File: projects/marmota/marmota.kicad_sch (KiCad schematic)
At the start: 51 parts, among them J1 USB_C, J2 Conn_01x20_Pin, J3 Conn_01x20_Pin, SW1 Button top, SW2 Button side, U1 RP2040, U2 FLASH, U3 MCP73871, U4 RT6160, U5 ESP32, Y1 12MHz

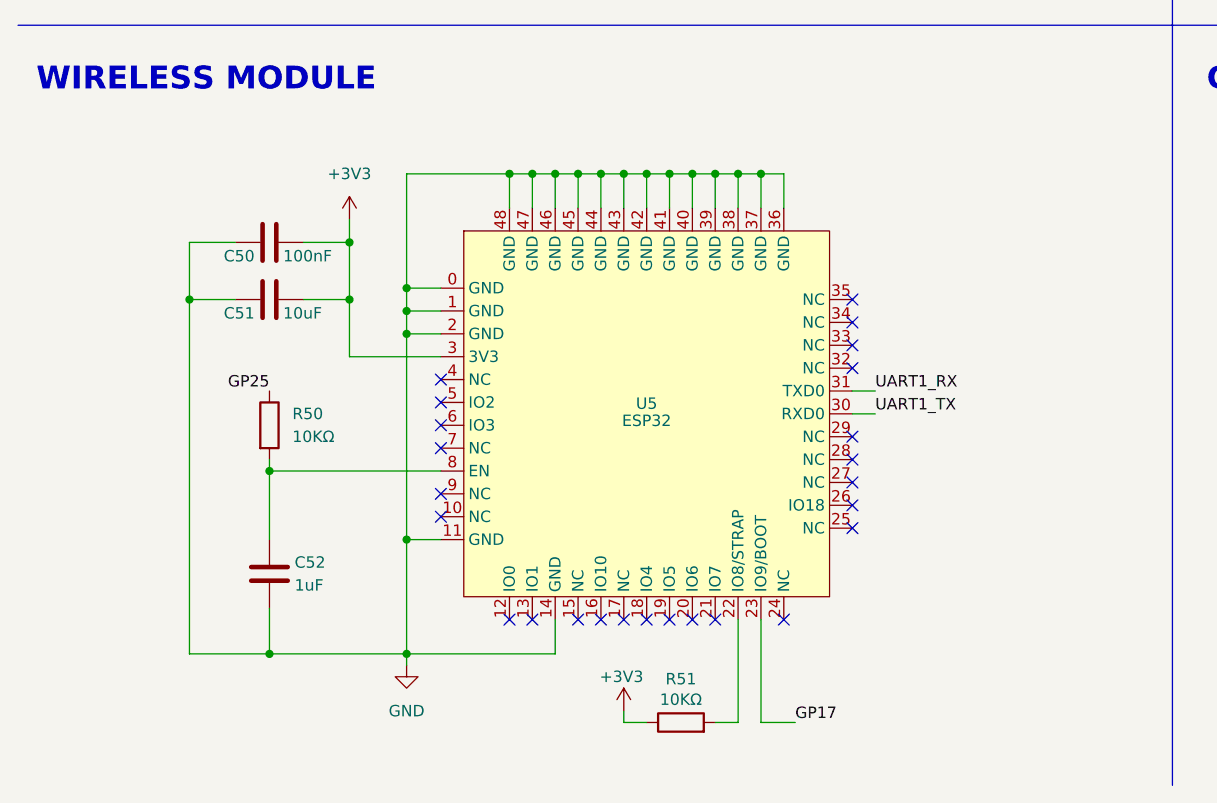
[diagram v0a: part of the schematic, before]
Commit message: Voltage divider and read on the ESP, Thermal relief for the ESP
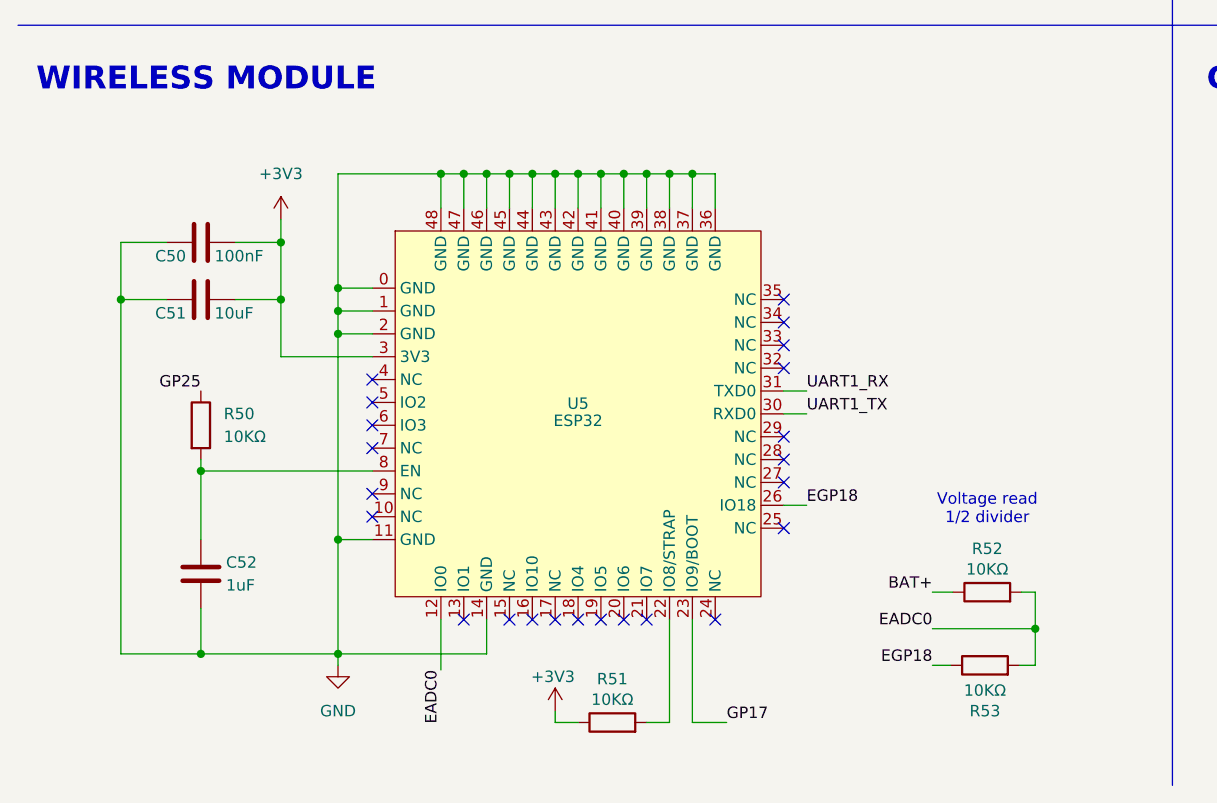
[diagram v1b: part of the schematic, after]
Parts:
- added R52, R53: 10KΩ, ILO_fp:0402_compact, symbol Device:R
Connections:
- net BAT+: now also R52.1
- net EADC0: now reaches U5.12 (IO0)
- net EADC0: now also R52.2, R53.2
- net EGP18: now reaches U5.26 (IO18)
- net EGP18: now also R53.1
- no-connect marks 37 -> 35
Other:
- note added: "Voltage read 1/2 divider"
- moved on the sheet: C50, C51, C52, R50, R51, U5

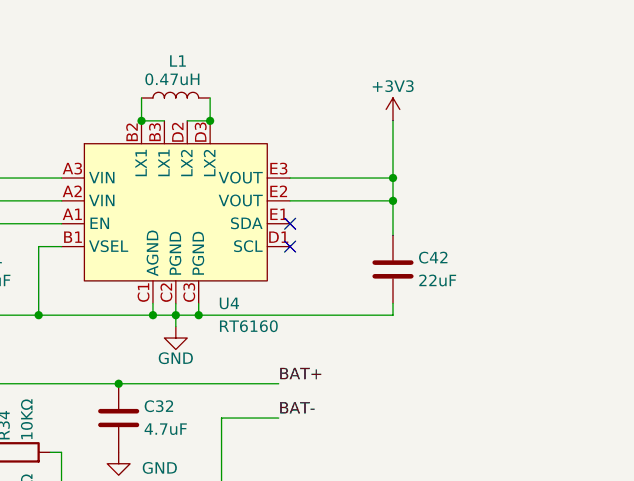
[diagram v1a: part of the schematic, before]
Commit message: New arrangement for buckboost, Added 2nd vcc capacitor
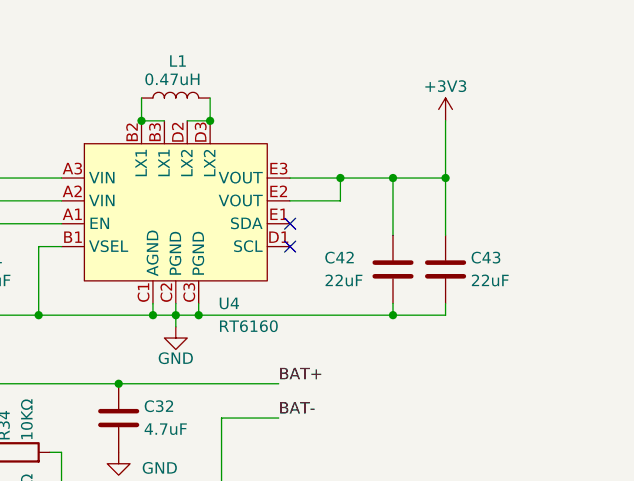
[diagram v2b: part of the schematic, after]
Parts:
- added C43: 22uF, ILO_fp:0402_compact, symbol Device:C
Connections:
- net +3V3: now also C43.2
- net GND: now also C43.1
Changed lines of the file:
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@@
 	)
 	(junction
+		(at 318.77 45.72)
+		(diameter 0)
+		(color 0 0 0 0)
+	)
+	(junction
 		(at 179.07 43.18)
 		(diameter 0)
@@
 	)
 	(junction
+		(at 312.928 30.48)
+		(diameter 0)
+		(color 0 0 0 0)
+	)
+	(junction
 		(at 279.4 45.72)
 		(diameter 0)
@@
 	)
 	(junction
-		(at 69.85 27.94)
+		(at 318.77 30.48)
 		(diameter 0)
 		(color 0 0 0 0)
 	)
 	(junction
-		(at 66.04 46.99)
+		(at 69.85 27.94)
 		(diameter 0)
 		(color 0 0 0 0)
 	)
 	(junction
-		(at 318.77 30.48)
+		(at 66.04 46.99)
 		(diameter 0)
 		(color 0 0 0 0)
@@
 	)
 	(junction
-		(at 318.77 33.02)
+		(at 324.612 30.48)
 		(diameter 0)
 		(color 0 0 0 0)
@@
 	(wire
 		(pts
+			(xy 324.612 30.48) (xy 324.612 36.83)
+		)
+		(stroke
+			(width 0)
+			(type default)
+		)
+	)
+	(wire
+		(pts
 			(xy 269.24 30.48) (xy 281.94 30.48)
 		)
@@
 	(wire
 		(pts
+			(xy 312.928 30.48) (xy 312.928 33.02)
+		)
+		(stroke
+			(width 0)
+			(type default)
+		)
+	)
+	(wire
+		(pts
 			(xy 182.88 26.67) (xy 182.88 27.94)
 		)
@@
 	(wire
 		(pts
-			(xy 318.77 30.48) (xy 318.77 33.02)
-		)
-		(stroke
-			(width 0)
-			(type default)
-		)
-	)
-	(wire
-		(pts
 			(xy 93.98 74.93) (xy 92.71 74.93)
 		)
@@
 	(wire
 		(pts
+			(xy 312.928 30.48) (xy 318.77 30.48)
+		)
+		(stroke
+			(width 0)
+			(type default)
+		)
+	)
+	(wire
+		(pts
 			(xy 68.58 46.99) (xy 71.12 46.99)
 		)
@@
 	(wire
 		(pts
+			(xy 318.77 30.48) (xy 318.77 36.83)
+		)
+		(stroke
+			(width 0)
+			(type default)
+		)
+	)
+	(wire
+		(pts
 			(xy 294.64 44.45) (xy 294.64 45.72)
 		)
@@
 	(wire
 		(pts
+			(xy 324.612 24.13) (xy 324.612 30.48)
+		)
+		(stroke
+			(width 0)
+			(type default)
+		)
+	)
+	(wire
+		(pts
 			(xy 64.77 166.37) (xy 64.77 170.18)
 		)
@@
 	(wire
 		(pts
+			(xy 307.34 33.02) (xy 312.928 33.02)
+		)
+		(stroke
+			(width 0)
+			(type default)
+		)
+	)
+	(wire
+		(pts
 			(xy 35.56 81.28) (xy 36.83 81.28)
 		)
@@
 	(wire
 		(pts
-			(xy 318.77 33.02) (xy 318.77 36.83)
-		)
-		(stroke
-			(width 0)
-			(type default)
-		)
-	)
-	(wire
-		(pts
 			(xy 237.49 63.5) (xy 234.95 63.5)
 		)
@@
 	(wire
 		(pts
-			(xy 307.34 30.48) (xy 318.77 30.48)
+			(xy 307.34 30.48) (xy 312.928 30.48)
 		)
 		(stroke
@@
 	(wire
 		(pts
-			(xy 307.34 33.02) (xy 318.77 33.02)
+			(xy 33.02 198.12) (xy 33.02 199.39)
 		)
 		(stroke
@@
 	(wire
 		(pts
-			(xy 33.02 198.12) (xy 33.02 199.39)
+			(xy 45.72 43.18) (xy 50.8 43.18)
 		)
 		(stroke
@@
 	(wire
 		(pts
-			(xy 45.72 43.18) (xy 50.8 43.18)
+			(xy 92.71 102.87) (xy 93.98 102.87)
 		)
 		(stroke
@@
 	(wire
 		(pts
-			(xy 92.71 102.87) (xy 93.98 102.87)
+			(xy 41.91 171.45) (xy 41.91 173.99)
 		)
 		(stroke
@@
 	(wire
 		(pts
-			(xy 41.91 171.45) (xy 41.91 173.99)
+			(xy 59.69 166.37) (xy 59.69 170.18)
 		)
 		(stroke
@@
 	(wire
 		(pts
-			(xy 59.69 166.37) (xy 59.69 170.18)
+			(xy 318.77 45.72) (xy 324.612 45.72)
 		)
 		(stroke
@@
 	(wire
 		(pts
+			(xy 324.612 45.72) (xy 324.612 44.45)
+		)
+		(stroke
+			(width 0)
+			(type default)
+		)
+	)
+	(wire
+		(pts
 			(xy 128.27 138.43) (xy 128.27 140.97)
 		)
@@
 	(wire
 		(pts
-			(xy 318.77 24.13) (xy 318.77 30.48)
-		)
-		(stroke
-			(width 0)
-			(type default)
-		)
-	)
-	(wire
-		(pts
 			(xy 124.206 212.852) (xy 125.73 212.852)
 		)
@@
 	(wire
 		(pts
+			(xy 318.77 30.48) (xy 324.612 30.48)
+		)
+		(stroke
+			(width 0)
+			(type default)
+		)
+	)
+	(wire
+		(pts
 			(xy 111.76 138.43) (xy 111.76 140.97)
 		)
@@
 	(symbol
 		(lib_id "power:+3V3")
-		(at 318.77 24.13 0)
+		(at 324.612 24.13 0)
 		(unit 1)
 		(exclude_from_sim no)
@@
 		(dnp no)
 		(property "Reference" "#PWR048"
-			(at 318.77 27.94 0)
+			(at 324.612 27.94 0)
 			(effects
 				(font
@@
 		)
 		(property "Value" "+3V3"
-			(at 318.77 20.32 0)
+			(at 324.612 20.32 0)
 			(effects
 				(font
@@
 		)
 		(property "Footprint" ""
-			(at 318.77 24.13 0)
+			(at 324.612 24.13 0)
 			(effects
 				(font
@@
 		)
 		(property "Datasheet" ""
-			(at 318.77 24.13 0)
+			(at 324.612 24.13 0)
 			(effects
 				(font
@@
 		)
 		(property "Description" "Power symbol creates a global label with name \"+3V3\""
-			(at 318.77 24.13 0)
+			(at 324.612 24.13 0)
 			(effects
 				(font
@@
 		(dnp no)
 		(property "Reference" "C42"
-			(at 321.564 39.37 0)
+			(at 311.15 39.37 0)
 			(effects
 				(font
@@
 		)
 		(property "Value" "22uF"
-			(at 321.564 41.91 0)
+			(at 311.15 41.91 0)
 			(effects
 				(font
@@
 					(unit 1)
 				)
+			)
+		)
+	)
+	(symbol
+		(lib_id "Device:C")
+		(at 324.612 40.64 180)
+		(unit 1)
+		(exclude_from_sim no)
+		(in_bom yes)
+		(on_board yes)
+		(dnp no)
+		(property "Reference" "C43"
+			(at 327.406 39.37 0)
+			(effects
+				(font
+					(size 1.27 1.27)
+				)
+				(justify right)
+			)
+		)
+		(property "Value" "22uF"
+			(at 327.406 41.91 0)
+			(effects
+				(font
+					(size 1.27 1.27)
+				)
+				(justify right)
+			)
+		)
+		(property "Footprint" "ILO_fp:0402_compact"
+			(at 323.6468 36.83 0)
+			(effects
+				(font
+					(size 1.27 1.27)
+				)
+				(hide yes)
+			)
+		)
+		(property "Datasheet" "~"
+			(at 324.612 40.64 0)
+			(effects
+				(font
+					(size 1.27 1.27)
+				)
+				(hide yes)
+			)
+		)
+		(property "Description" "Unpolarized capacitor"
+			(at 324.612 40.64 0)
+			(effects
+				(font
+					(size 1.27 1.27)
+				)
+				(hide yes)
+			)
+		)
+		(property "LCSC" "C105226"
+			(at 324.612 40.64 0)
+			(effects
+				(font
+					(size 1.27 1.27)
+				)
+				(hide yes)
+			)
+		)
+		(property "Export" "yes"
+			(at 324.612 40.64 0)
+			(effects
+				(font
+					(size 1.27 1.27)
+				)
+				(hide yes)
+			)
+		)
+		(property "Group" "C"
+			(at 324.612 40.64 0)
+			(effects
+				(font
+					(size 1.27 1.27)
+				)
+				(hide yes)
+			)
+		)
+		(property "Mount" "SMD"
+			(at 324.612 40.64 0)
+			(effects
+				(font
+					(size 1.27 1.27)
+				)
+				(hide yes)
+			)
+		)
+		(pin "2"
+		)
+		(pin "1"
+		)
+		(instances
+			(project "marmota"
+				(path "/752a740b-2d20-4431-a887-abcf944e2ab4"
+					(reference "C43")
+					(unit 1)
+				)

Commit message: Added I2C pullups
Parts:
- added R7, R8: 4.7KΩ, ILO_fp:0402_compact, symbol Device:R
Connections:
- net +3V3: now also R7.2, R8.2
- net I2C_SCL: now also R8.1
- net I2C_SDA: now also R7.1
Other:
- note added: "Analog filtering"
- note added: "Board LED"
- note added: "Controlled from RP2040"
- note added: "Flash and comms from/to RP2040"
- note added: "I2C pull-up"
- note added: "Reset"
- moved on the sheet: C50, C51, C61, C62, C63, C64, D1, R6

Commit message: Bigger footprint inductor
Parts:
- L1: footprint ILO_fp:0603_compact -> ILO_fp:SMD_16x10; LCSC C341701 -> C5832340
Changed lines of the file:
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@@
 			)
 		)
-		(property "Footprint" "ILO_fp:0603_compact"
+		(property "Footprint" "ILO_fp:SMD_16x10"
 			(at 294.64 21.59 0)
 			(effects
@@
 			)
 		)
-		(property "LCSC" "C341701"
+		(property "LCSC" "C5832340"
 			(at 294.64 21.59 0)
 			(effects

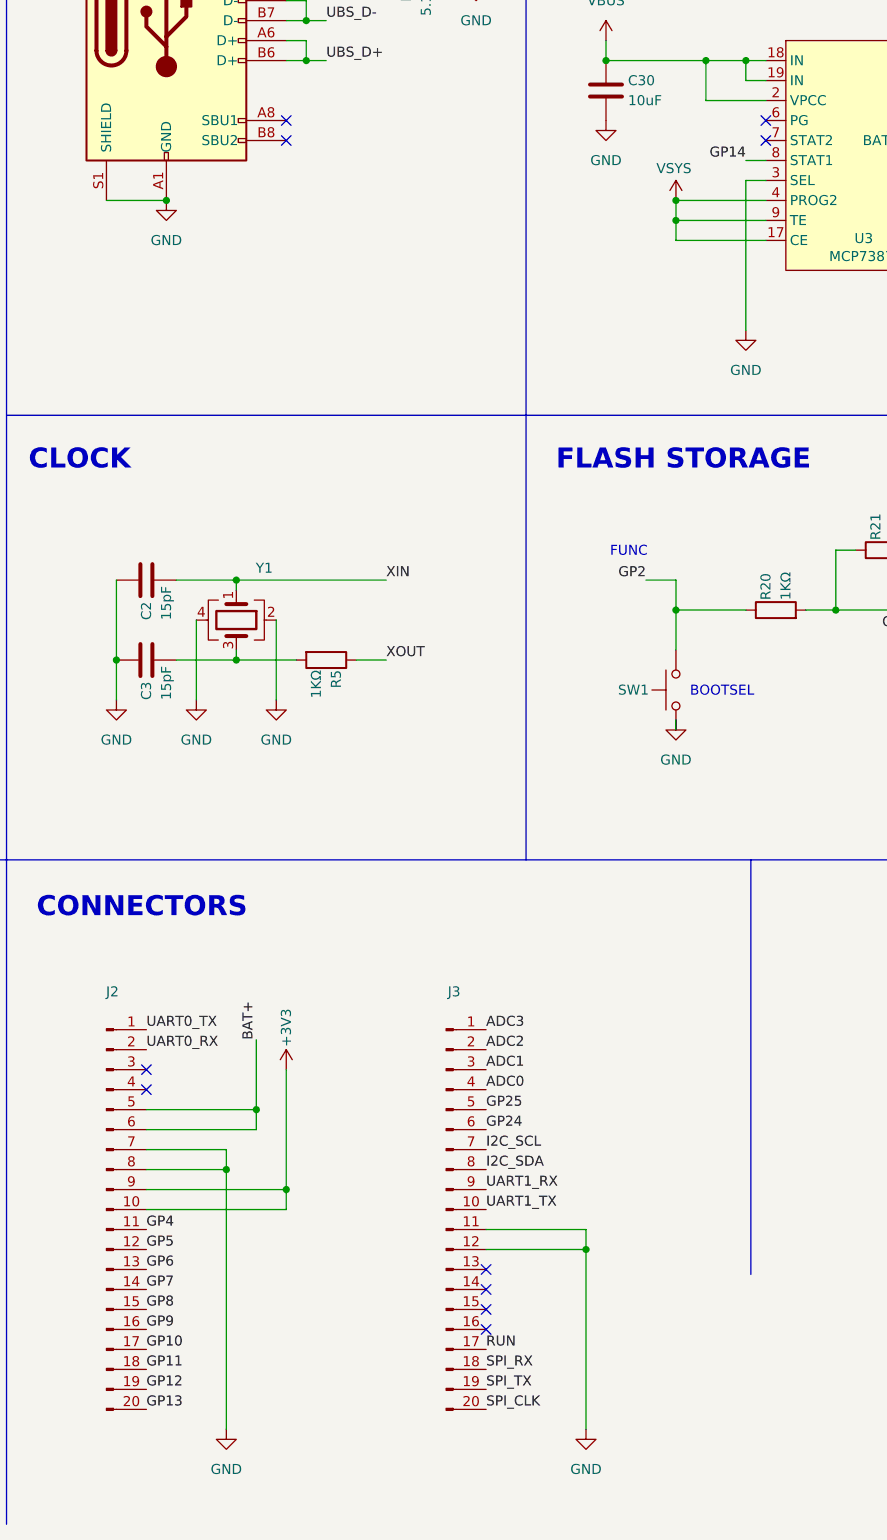
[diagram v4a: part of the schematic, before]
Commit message: Extra GPIO exposed to connector, Ground plane tweaks
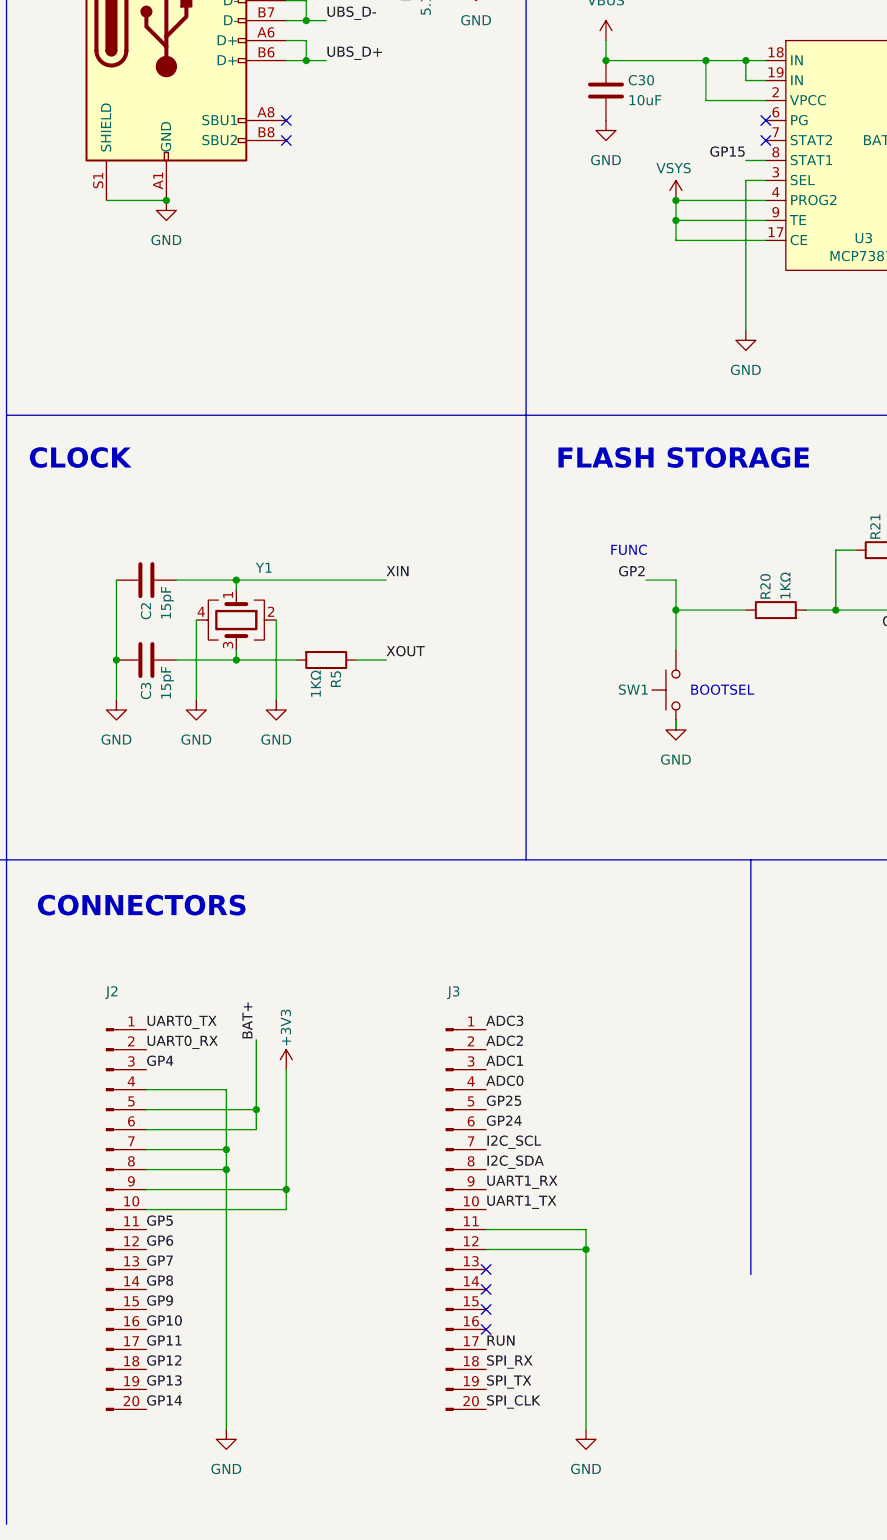
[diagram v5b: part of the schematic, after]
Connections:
- net GND: now also J2.4 (Pin_4)
- net GP10: now also J2.16 (Pin_16); no longer J2.17 (Pin_17)
- net GP11: now also J2.17 (Pin_17); no longer J2.18 (Pin_18)
- net GP12: now also J2.18 (Pin_18); no longer J2.19 (Pin_19)
- net GP13: now also J2.19 (Pin_19); no longer J2.20 (Pin_20)
- net GP14: now also J2.20 (Pin_20); no longer U3.8 (STAT1)
- net GP15: now also U3.8 (STAT1)
- net GP4: now also J2.3 (Pin_3); no longer J2.11 (Pin_11)
- net GP5: now also J2.11 (Pin_11); no longer J2.12 (Pin_12)
- net GP6: now also J2.12 (Pin_12); no longer J2.13 (Pin_13)
- net GP7: now also J2.13 (Pin_13); no longer J2.14 (Pin_14)
- net GP8: now also J2.14 (Pin_14); no longer J2.15 (Pin_15)
- net GP9: now also J2.15 (Pin_15); no longer J2.16 (Pin_16)
- no-connect marks 35 -> 33
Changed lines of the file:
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@@
 	)
 	(junction
+		(at 168.91 186.69)
+		(diameter 0)
+		(color 0 0 0 0)
+	)
+	(junction
 		(at 63.5 46.99)
 		(diameter 0)
@@
 	)
 	(no_connect
-		(at 158.75 179.07)
-	)
-	(no_connect
 		(at 237.49 55.88)
 	)
@@
 	)
 	(no_connect
-		(at 158.75 176.53)
-	)
-	(no_connect
 		(at 52.07 196.85)
 	)
@@
 	(wire
 		(pts
+			(xy 168.91 179.07) (xy 168.91 186.69)
+		)
+		(stroke
+			(width 0)
+			(type default)
+		)
+	)
+	(wire
+		(pts
 			(xy 87.63 166.37) (xy 87.63 170.18)
 		)
@@
 	(wire
 		(pts
+			(xy 158.75 179.07) (xy 168.91 179.07)
+		)
+		(stroke
+			(width 0)
+			(type default)
+		)
+	)
+	(wire
+		(pts
 			(xy 92.71 135.89) (xy 113.03 135.89)
 		)
@@
 		)
 	)
-	(label "GP11"
+	(label "GP12"
 		(at 158.75 214.63 0)
 		(fields_autoplaced yes)
@@
 		)
 	)
-	(label "GP13"
+	(label "GP14"
 		(at 158.75 219.71 0)
 		(fields_autoplaced yes)
@@
 		)
 	)
-	(label "GP6"
+	(label "GP7"
 		(at 158.75 201.93 0)
 		(fields_autoplaced yes)
@@
 		)
 	)
+	(label "GP4"
+		(at 158.75 176.53 0)
+		(fields_autoplaced yes)
+		(effects
+			(font
+				(size 1.27 1.27)
+			)
+			(justify left bottom)
+		)
+	)
 	(label "GP11"
 		(at 93.98 92.71 0)
@@
 		)
 	)
-	(label "GP5"
+	(label "GP6"
 		(at 158.75 199.39 0)
 		(fields_autoplaced yes)
@@
 		)
 	)
-	(label "GP7"
+	(label "GP8"
 		(at 158.75 204.47 0)
 		(fields_autoplaced yes)
@@
 		)
 	)
-	(label "GP8"
+	(label "GP9"
 		(at 158.75 207.01 0)
 		(fields_autoplaced yes)
@@
 		)
 	)
-	(label "GP4"
+	(label "GP5"
 		(at 158.75 196.85 0)
 		(fields_autoplaced yes)
@@
 		)
 	)
-	(label "GP9"
+	(label "GP10"
 		(at 158.75 209.55 0)
 		(fields_autoplaced yes)
@@
 		)
 	)
-	(label "GP14"
+	(label "GP15"
 		(at 234.95 60.96 180)
 		(fields_autoplaced yes)
@@
 		)
 	)
-	(label "GP12"
+	(label "GP13"
 		(at 158.75 217.17 0)
 		(fields_autoplaced yes)
@@
 		)
 	)
-	(label "GP10"
+	(label "GP11"
 		(at 158.75 212.09 0)
 		(fields_autoplaced yes)
